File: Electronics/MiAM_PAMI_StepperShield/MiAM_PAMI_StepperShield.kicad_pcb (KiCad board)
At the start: 2 copper layers, 43.7 x 54.2 mm, 18 parts, among them J2 Conn_01x05_Male, U1 ESP32-DEVKIT-V1

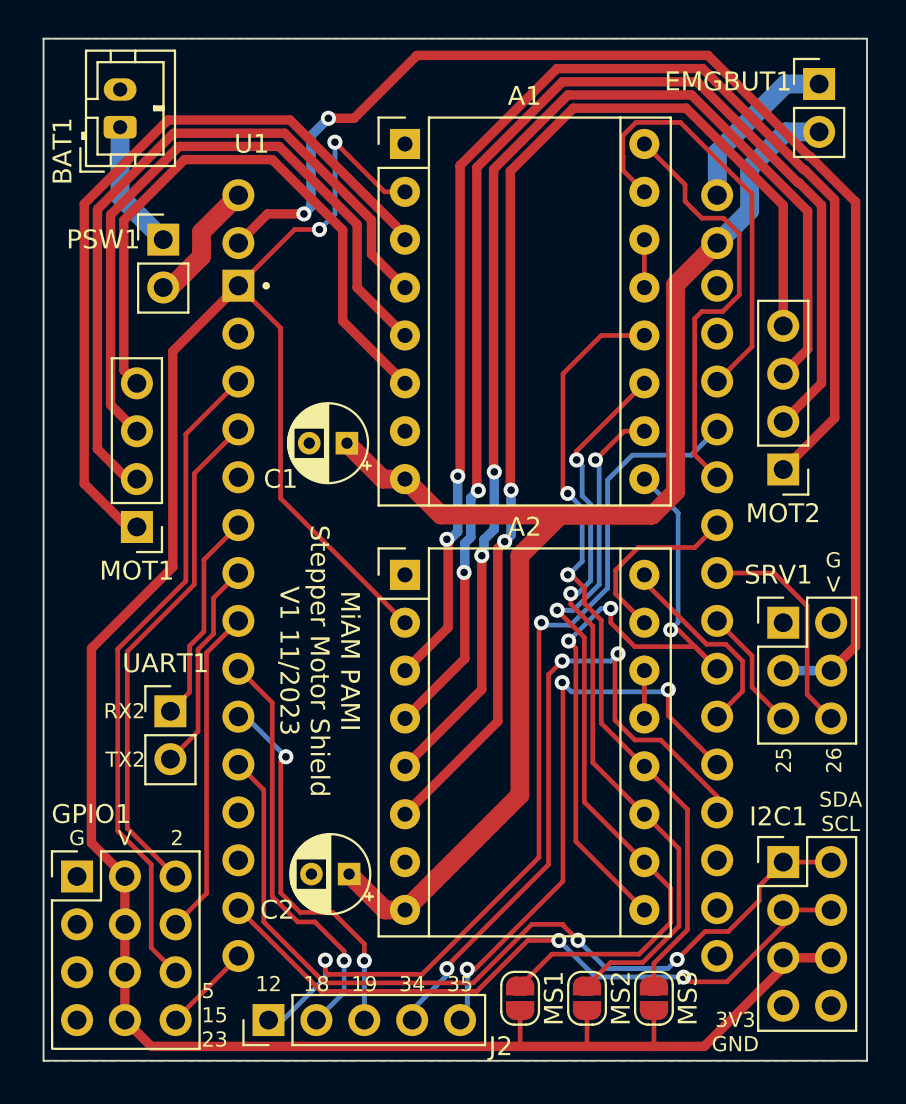
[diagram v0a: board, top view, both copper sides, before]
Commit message: Fix shield footprint
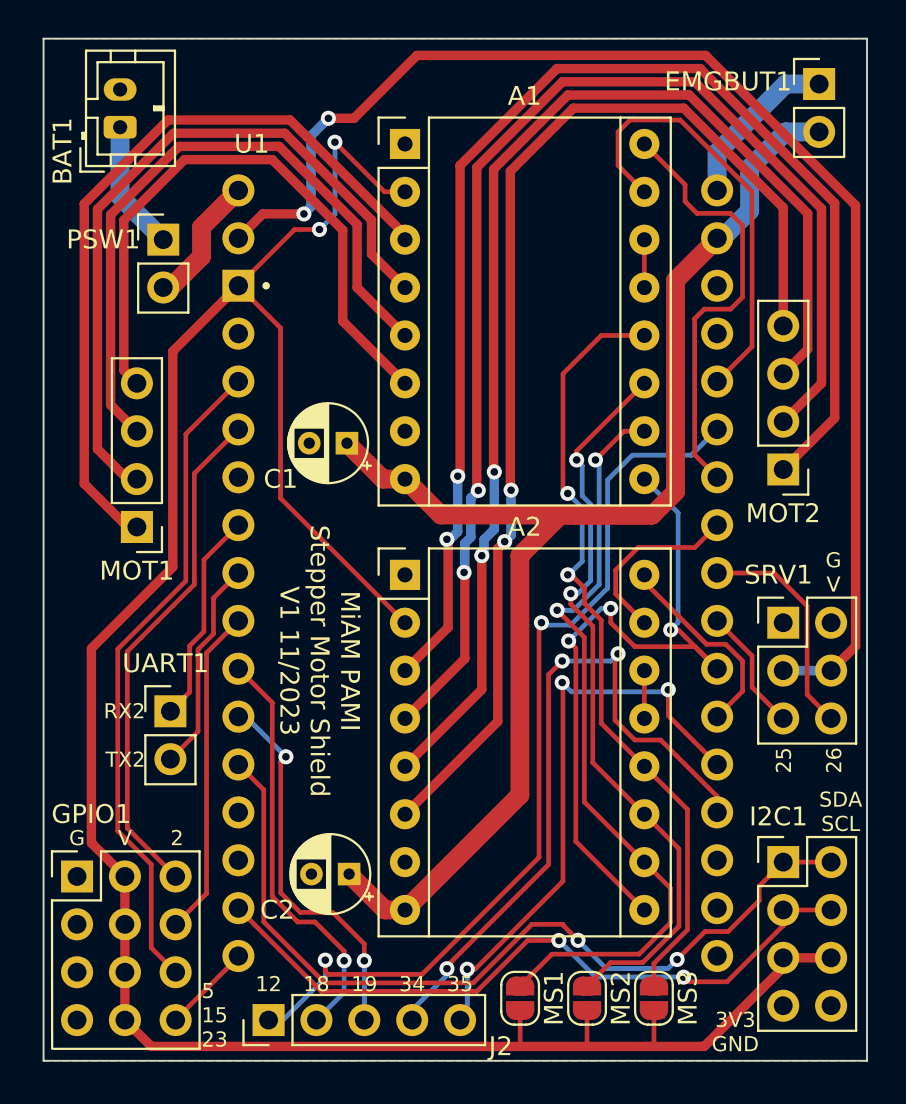
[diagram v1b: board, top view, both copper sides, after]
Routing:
- net /DIR_1: track 22.6 -> 23.2 mm
- net /STEP_1: track 22.9 -> 23.5 mm
